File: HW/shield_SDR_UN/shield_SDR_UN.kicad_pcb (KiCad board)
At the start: 2 copper layers, 100 x 100 mm, 221 parts, among them J1 Conn_02x09_Odd_Even, J2 Conn_02x08_Odd_Even, J3 Conn_02x10_Top_Bottom, J4 USB_B_Micro, J5 USB_A, J6 Conn_02x06_Odd_Even, P1 GSG-RF-CONN, P2 GSG-RF-CONN, Q1 MOSFET_P, T1 BALUN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

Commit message: PCB route V2
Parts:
- moved R55 6.41 mm to (301.1, 78.6)
- moved C109 4.84 mm to (300.9, 77.1)
- moved C73 4.38 mm to (300.9, 99.0)
- moved C80 4.32 mm to (300.9, 97.5)
- moved C64 4.30 mm to (296.4, 106.0), turned to 0 degrees
- moved C79 4.29 mm to (300.9, 95.9)
- moved C78 2.66 mm to (302.2, 93.2)
- moved C70 2.14 mm to (277.8, 105.9)
- moved C76 2.14 mm to (285.3, 105.9)
- moved C56 2.14 mm to (282.3, 105.9)
- moved C57 2.14 mm to (283.8, 105.9)
- moved C58 2.14 mm to (280.8, 105.9)
- moved C60 2.14 mm to (279.3, 105.9)
- moved C108 1.47 mm to (302.2, 89.9)
- moved C59 1.19 mm to (276.3, 105.9)
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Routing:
- net /FPGA/FPGA_GPIO_00: track 0.00 -> 34.5 mm, vias 0 -> 2
- net /FPGA/FPGA_GPIO_01: track 0.00 -> 33.5 mm, vias 0 -> 2
- net /FPGA/FPGA_GPIO_02: track 0.00 -> 31.6 mm, vias 0 -> 2
- net I2C_SDA: track 24.0 -> 49.9 mm, vias 0 -> 3
- net 3V3 FPGA: track 0.00 -> 24.3 mm
- net I2C_SCL: track 20.6 -> 42.7 mm, vias 0 -> 3
- net /FPGA/FPGA_GPIO_03: track 13.6 -> 29.8 mm, vias 1 -> 2
- net /FPGA/FPGA_GPIO_19: track 0.00 -> 16.1 mm, vias 0 -> 2
- net /FPGA/FPGA_GPIO_18: track 0.00 -> 16.0 mm, vias 0 -> 2
- net /FPGA/FPGA_GPIO_16: track 0.00 -> 15.3 mm, vias 0 -> 2
- net /FPGA/FPGA_GPIO_20: track 0.00 -> 15.3 mm, vias 0 -> 2
- net /FPGA/FPGA_GPIO_14: track 0.00 -> 15.2 mm, vias 0 -> 2
- net /FPGA/FPGA_GPIO_21: track 0.00 -> 14.9 mm, vias 0 -> 2
- net /FPGA/FPGA_GPIO_17: track 0.00 -> 14.8 mm, vias 0 -> 2
- net /FPGA/FPGA_GPIO_15: track 0.00 -> 14.7 mm, vias 0 -> 2
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
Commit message: PCB routing
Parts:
- moved R3 0.14 mm to (237.9, 72.6), turned to 270 degrees
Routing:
- net /proc/LED2: track 0.00 -> 10.5 mm
- net /proc/LED1: track 0.00 -> 10.3 mm
- net 1V2 FPGA: track 5.49 -> 14.5 mm
- net 3V3 FPGA: track 24.3 -> 33.2 mm
- net /rf_front_end/RXBBI+: track 0.00 -> 5.61 mm
- net /rf_front_end/RXBBI-: track 0.00 -> 5.19 mm
- net /rf_front_end/RXBBQ-: track 0.00 -> 4.07 mm
- net /rf_front_end/RXBBQ+: track 0.00 -> 3.65 mm
- net /omega_2/BOOT_0: track 3.44 -> 0.04 mm
- net Net-(D6-Pad2): track 0.00 -> 2.05 mm
- net Net-(D9-Pad2): track 0.00 -> 2.05 mm
- net SPI1_MISO: track 0.00 -> 2.02 mm
- net Net-(D5-Pad2): track 0.00 -> 2.01 mm
- net Net-(D8-Pad2): track 0.00 -> 1.92 mm
- net Net-(D7-Pad2): track 0.00 -> 1.82 mm
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
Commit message: PCB route V3
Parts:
- R53: moved to B.Cu
- moved C102 155.3 mm to (115.7, 82.4)
- moved C95 155.0 mm to (116.0, 70.9)
- moved U4 155.0 mm to (131.7, 78.7)
- moved U5 155.0 mm to (131.7, 78.7)
- moved BT1 155.0 mm to (158.9, 55.0)
- moved C1 155.0 mm to (115.6, 41.9)
- moved C10 155.0 mm to (103.7, 61.9)
- moved C103 155.0 mm to (123.0, 57.9)
- moved C106 155.0 mm to (127.5, 96.3)
- moved C108 155.0 mm to (147.7, 77.9)
- moved C109 155.0 mm to (146.4, 65.2)
- moved C112 155.0 mm to (137.9, 62.8)
- moved C113 155.0 mm to (153.5, 127.0)
- moved C116 155.0 mm to (158.8, 127.0)
- moved C117 155.0 mm to (138.6, 124.0)
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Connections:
- R3 pad 2: SPI1_MOSI -> /proc/SPI1_MOSI
- U4 pad 112: /proc/FMC_NBL0 -> FMC_NBL0
- U4 pad 132: /proc/FMC_NWAIT -> FMC_NWAIT
- U4 pad 133: /proc/FMC_NWE -> FMC_NWE
- U4 pad 44: /proc/FMC_D10 -> FMC_D10
- U5 pad 1: /FPGA/FMC_A23 -> FMC_A23
- U5 pad 114: /FPGA/FMC_D2 -> FMC_D2
- U5 pad 115: /FPGA/FMC_D3 -> FMC_D3
- U5 pad 117: /FPGA/FMC_CLK -> FMC_CLK
- U5 pad 118: /FPGA/FMC_NOE -> FMC_NOE
- U5 pad 123: /FPGA/FMC_NE1 -> FMC_NE1
- U5 pad 137: /FPGA/FMC_NL -> FMC_NL
- U5 pad 142: /FPGA/FMC_NBL1 -> FMC_NBL1
- U5 pad 2: /FPGA/FMC_A19 -> FMC_A19
- U5 pad 3: /FPGA/FMC_A20 -> FMC_A20
- U5 pad 4: /FPGA/FMC_A21 -> FMC_A21
- U5 pad 43: /rf_front_end/SPI1_MOSI -> SPI1_MOSI
- U5 pad 5: /FPGA/FMC_A22 -> FMC_A22
- U5 pad 58: /FPGA/FMC_D4 -> FMC_D4
- U5 pad 59: /FPGA/FMC_D5 -> FMC_D5
- U5 pad 60: /FPGA/FMC_D6 -> FMC_D6
- U5 pad 63: /FPGA/FMC_D7 -> FMC_D7
- U5 pad 64: /FPGA/FMC_D8 -> FMC_D8
- U5 pad 65: /FPGA/FMC_D9 -> FMC_D9
- U5 pad 67: /FPGA/FMC_D11 -> FMC_D11
- U5 pad 68: /FPGA/FMC_D12 -> FMC_D12
- U5 pad 77: /FPGA/FMC_D13 -> FMC_D13
- U5 pad 78: /FPGA/FMC_D14 -> FMC_D14
- U5 pad 79: /FPGA/FMC_D15 -> FMC_D15
- U5 pad 80: /FPGA/FMC_A16 -> FMC_A16
- U5 pad 81: /FPGA/FMC_A17 -> FMC_A17
- U5 pad 82: /FPGA/FMC_A18 -> FMC_A18
- U5 pad 85: /FPGA/FMC_D0 -> FMC_D0
- U5 pad 86: /FPGA/FMC_D1 -> FMC_D1
- U5 pad 89: /FPGA/FMC_A14 -> FMC_A14
- U5 pad 90: /FPGA/FMC_A15 -> FMC_A15
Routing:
- net 3V3 FPGA: track 33.2 -> 79.8 mm
- net 3V3 MCU: track 1.64 -> 35.7 mm
- net 1V2 FPGA: track 14.5 -> 23.1 mm
- net /FPGA/DONE: track 0.00 -> 8.38 mm, vias 0 -> 1
- net FMC_A21: track 0.00 -> 8.22 mm, vias 0 -> 1
- net FMC_A17: track 0.00 -> 7.73 mm, vias 0 -> 1
- net FMC_A14: track 0.00 -> 7.49 mm, vias 0 -> 1
- net FMC_NWE: track 0.00 -> 7.31 mm, vias 0 -> 1
- net FMC_A15: track 0.00 -> 7.30 mm, vias 0 -> 1
- net FMC_A16: track 0.00 -> 7.30 mm, vias 0 -> 1
- net FMC_A19: track 0.00 -> 7.28 mm, vias 0 -> 1
- net FMC_A20: track 0.00 -> 7.21 mm, vias 0 -> 1
- net FMC_D15: track 0.00 -> 7.09 mm, vias 0 -> 1
- net FMC_D14: track 0.00 -> 7.09 mm, vias 0 -> 1
- net FMC_D13: track 0.00 -> 7.09 mm, vias 0 -> 1
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
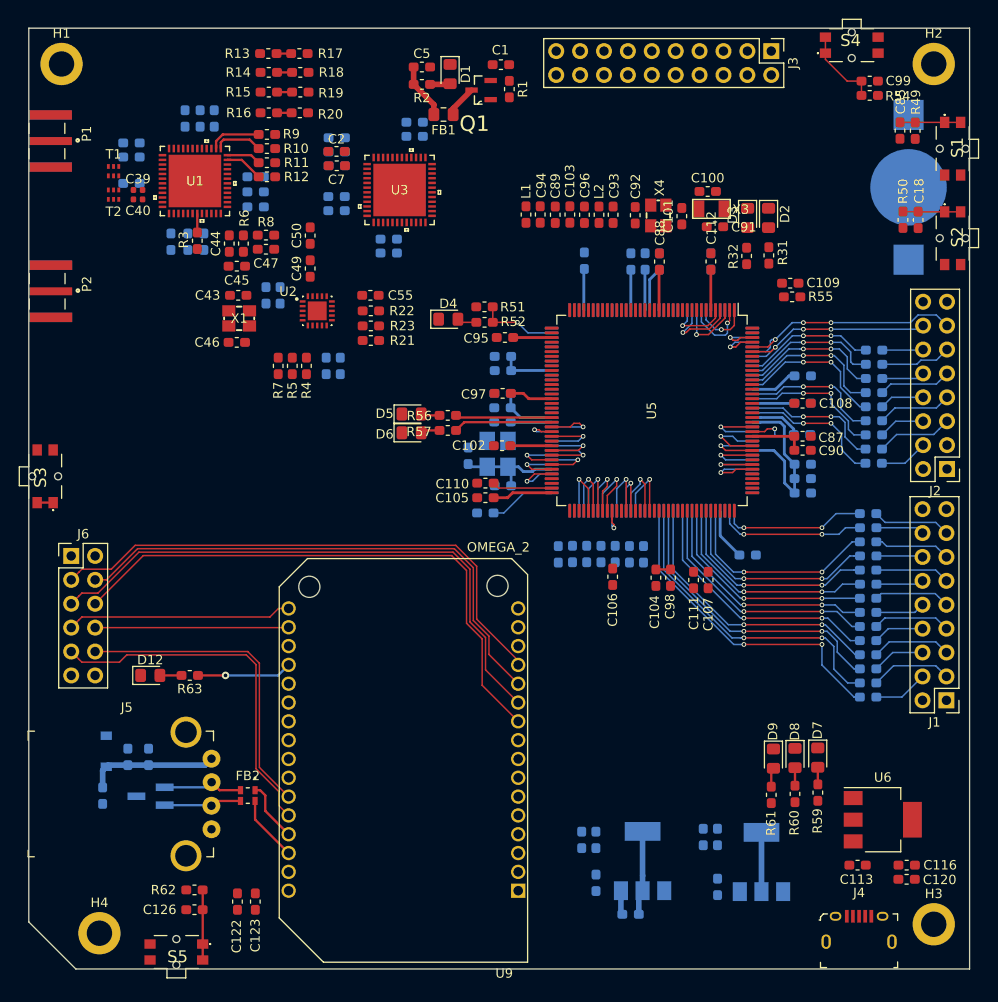
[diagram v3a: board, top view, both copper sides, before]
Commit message: PCB, Power stage routed
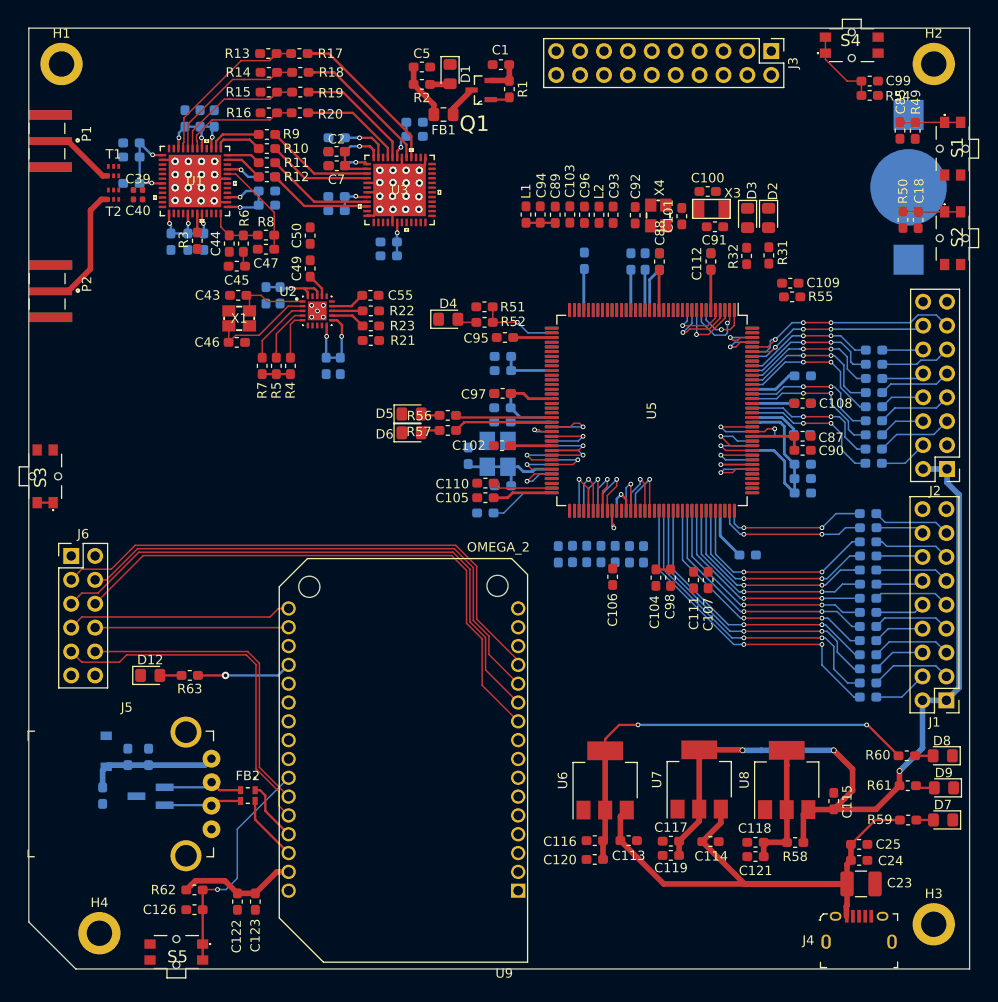
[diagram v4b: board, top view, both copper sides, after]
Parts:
- added C23: 220uF, Resistor_SMD:R_1210_3225Metric_Pad1.42x2.65mm_HandSolder, F.Cu at (153.9, 129.0)
- added C24: 100nF, Capacitor_SMD:C_0603_1608Metric_Pad1.05x0.95mm_HandSolder, F.Cu at (153.7, 126.5)
- added C25: 1nF, Capacitor_SMD:C_0603_1608Metric_Pad1.05x0.95mm_HandSolder, F.Cu at (153.7, 124.8)
- C114, C115, C117, C118, C119, C121, R58, U7, U8: moved to F.Cu
- moved C116 33.3 mm to (125.6, 124.4)
- moved C120 33.2 mm to (125.6, 126.4)
- moved U6 29.8 mm to (126.7, 118.0), turned to 90 degrees
- moved C115 26.7 mm to (151.0, 120.2)
- moved C113 24.5 mm to (129.2, 124.4)
- moved R58 19.1 mm to (146.9, 124.6), turned to 0 degrees
- moved C121 18.6 mm to (142.7, 126.1), turned to 180 degrees
- moved D9 18.4 mm to (162.7, 118.8), turned to 180 degrees
- moved U8 17.6 mm to (146.0, 118.0)
- moved C118 17.0 mm to (142.7, 124.6), turned to 180 degrees
- moved D8 15.7 mm to (162.6, 115.4), turned to 180 degrees
- moved D7 14.9 mm to (162.6, 122.2), turned to 180 degrees
- moved R61 14.5 mm to (158.9, 118.6), turned to 0 degrees
- moved R60 12.6 mm to (158.8, 115.4), turned to 0 degrees
- moved U7 11.0 mm to (136.7, 117.9)
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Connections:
- net /FPGA/FPGA_JTDO renamed /FPGA_JTDO
- net /omega_2/BOOT_0 renamed /BOOT_0
- net /omega_2/OMG_JNRST renamed /OMG_JNRST
- net /omega_2/OMG_JTCK renamed /OMG_JTCK
- net /omega_2/OMG_JTDI renamed /OMG_JTDI
- net /omega_2/OMG_JTMS renamed /OMG_JTMS
- net /omega_2/OMG_JTRST renamed /OMG_JTRST
- net /proc/STM_JTDO renamed /STM_JTDO
- R3 pad 2: /proc/SPI1_MOSI -> SPI1_MOSI
- R4 pad 2: /omega_2/I2C1_SDA -> I2C_SCL
- R5 pad 2: /omega_2/I2C1_SCL -> I2C_SDA
- U2 pad 4: /omega_2/I2C1_SCL -> I2C_SDA
- U2 pad 5: /omega_2/I2C1_SDA -> I2C_SCL
- U5 pad 40: /rf_front_end/SPI1_CS_RF -> SPI1_CS_RF
- U5 pad 41: /rf_front_end/SPI1_SCK -> SPI1_SCK
- U5 pad 42: /rf_front_end/SPI1_MISO -> SPI1_MISO
- U5 pad 44: /rf_front_end/SPI1_CS_AD -> SPI1_CS_AD
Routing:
- net 3V3 MCU: track 35.7 -> 125.5 mm, vias 0 -> 6
- net 3V3 FPGA: track 79.8 -> 160.6 mm, vias 0 -> 3
- net +5V: track 0.00 -> 65.4 mm
- net VAA: track 5.94 -> 57.3 mm, vias 0 -> 12
- net GND: track 0.00 -> 36.1 mm, vias 0 -> 37
- net /rf_front_end/QD+: track 0.00 -> 18.4 mm
- net /omega_2/RST_BTN: track 7.45 -> 24.6 mm, vias 0 -> 1
- net /rf_front_end/TXBBI+: track 1.55 -> 17.5 mm
- net /rf_front_end/QD-: track 0.00 -> 15.0 mm
- net /rf_front_end/TXBBI-: track 1.60 -> 16.1 mm
- net Net-(P2-Pad1): track 0.00 -> 13.7 mm
- net /rf_front_end/TXBBQ+: track 1.60 -> 14.5 mm
- net /rf_front_end/ID-: track 0.00 -> 12.8 mm
- net /rf_front_end/IA+: track 0.00 -> 11.5 mm
- net /rf_front_end/QA-: track 0.00 -> 11.5 mm
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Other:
- rule via_min_size: 0.4 -> 0.3

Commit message: PCB routing
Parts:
- moved D5 5.85 mm to (112.0, 79.3)
- moved D6 5.85 mm to (112.0, 81.3)
- moved R56 5.85 mm to (115.8, 79.5)
- moved R57 5.85 mm to (115.8, 81.1)
- moved C65 2.40 mm to (113.8, 79.7)
- moved C66 2.40 mm to (113.8, 81.2)
- moved X2 2.40 mm to (113.2, 84.6)
- moved C63 2.40 mm to (113.8, 88.0)
- moved C71 2.40 mm to (113.8, 78.1)
- moved C84 2.40 mm to (110.1, 84.8)
- moved C102 1.15 mm to (115.7, 83.6)
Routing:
- net adDA0: track 0.00 -> 34.2 mm, vias 0 -> 1
- net adDA1: track 0.00 -> 33.5 mm, vias 0 -> 1
- net adDA2: track 0.00 -> 32.8 mm, vias 0 -> 1
- net adDA3: track 0.00 -> 32.1 mm, vias 0 -> 1
- net adDA4: track 0.00 -> 31.1 mm, vias 0 -> 1
- net I2C_SCL: track 47.9 -> 78.5 mm, vias 3 -> 4
- net adDA5: track 0.00 -> 30.4 mm, vias 0 -> 1
- net adDA6: track 0.00 -> 29.7 mm, vias 0 -> 1
- net I2C_SDA: track 56.0 -> 84.7 mm, vias 3 -> 4
- net adDA7: track 0.00 -> 28.6 mm, vias 0 -> 1
- net adDD2: track 0.00 -> 26.8 mm, vias 0 -> 1
- net adDD0: track 0.00 -> 26.6 mm, vias 0 -> 1
- net adDD1: track 0.00 -> 25.9 mm, vias 0 -> 1
- net adDD3: track 0.00 -> 25.8 mm, vias 0 -> 1
- net adDD4: track 0.00 -> 25.2 mm, vias 0 -> 1
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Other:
- board text added: "Profe vea esta belleza, pongame 5"
- board text removed: "Camargo vea esta belleza, pongame 5"

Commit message: PCB route V4
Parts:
- C88: moved to B.Cu
- moved C112 7.19 mm to (144.9, 60.9)
- moved C74 7.18 mm to (144.9, 60.9)
- moved X2 6.75 mm to (107.8, 80.6)
- moved X3 5.76 mm to (141.9, 61.5)
- moved C92 5.56 mm to (134.9, 60.3), turned to 90 degrees
- moved C91 4.87 mm to (143.2, 58.6), turned to 90 degrees
- moved D2 4.80 mm to (148.9, 58.2)
- moved R31 4.80 mm to (148.9, 62.2)
- moved D3 4.80 mm to (146.6, 58.2)
- moved R32 4.80 mm to (146.5, 62.2)
- moved C100 4.37 mm to (140.5, 58.7), turned to 90 degrees
- moved C84 4.21 mm to (114.0, 86.4), turned to 180 degrees
- moved C89 4.16 mm to (121.9, 62.0)
- moved L1 4.16 mm to (118.8, 62.0)
- moved C94 4.16 mm to (120.3, 62.0)
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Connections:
- net /BOOT_0 renamed /omega_2/BOOT_0
- net /FPGA_JTDO renamed /FPGA/FPGA_JTDO
- net /OMG_JNRST renamed /omega_2/OMG_JNRST
- net /OMG_JTCK renamed /omega_2/OMG_JTCK
- net /OMG_JTDI renamed /omega_2/OMG_JTDI
- net /OMG_JTMS renamed /omega_2/OMG_JTMS
- net /OMG_JTRST renamed /omega_2/OMG_JTRST
- net /STM_JTDO renamed /proc/STM_JTDO
- J3 pad 10: GND -> /proc/GPIO_MCU_8
- J3 pad 11: 3V3 MCU -> /proc/GPIO_MCU_9
- J3 pad 12: /proc/GPIO_MCU_9 -> /proc/GPIO_MCU_10
- J3 pad 13: /proc/GPIO_MCU_10 -> /proc/GPIO_MCU_11
- J3 pad 14: /proc/GPIO_MCU_11 -> /proc/GPIO_MCU_12
- J3 pad 15: /proc/GPIO_MCU_12 -> /proc/GPIO_MCU_13
- J3 pad 16: /proc/GPIO_MCU_13 -> /proc/GPIO_MCU_14
- J3 pad 17: /proc/GPIO_MCU_14 -> /proc/GPIO_MCU_15
- J3 pad 18: /proc/GPIO_MCU_15 -> Net-(J3-Pad18)
- J3 pad 19: /proc/GPIO_MCU_16 -> GND
- J3 pad 2: /proc/GPIO_MCU_1 -> 3V3 MCU
- J3 pad 3: /proc/GPIO_MCU_2 -> /proc/GPIO_MCU_1
- J3 pad 4: /proc/GPIO_MCU_3 -> /proc/GPIO_MCU_2
- J3 pad 5: /proc/GPIO_MCU_4 -> /proc/GPIO_MCU_3
- J3 pad 6: /proc/GPIO_MCU_5 -> /proc/GPIO_MCU_4
- J3 pad 7: /proc/GPIO_MCU_6 -> /proc/GPIO_MCU_5
- J3 pad 8: /proc/GPIO_MCU_7 -> /proc/GPIO_MCU_6
- J3 pad 9: /proc/GPIO_MCU_8 -> /proc/GPIO_MCU_7
- R4 pad 2: I2C_SCL -> I2C_SDA
- R5 pad 2: I2C_SDA -> I2C_SCL
- U2 pad 4: I2C_SDA -> I2C_SCL
- U2 pad 5: I2C_SCL -> I2C_SDA
- U5 pad 136: /proc/GPIO_MCU_16 -> Net-(U5-Pad136)
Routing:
- net /omega_2/OMG_JNRST: track 8.67 -> 163.2 mm, vias 0 -> 5
- net /omega_2/OMG_JTMS: track 0.00 -> 140.5 mm, vias 0 -> 3
- net /FPGA/FPGA_JTDO: track 0.00 -> 115.1 mm, vias 0 -> 6
- net /omega_2/OMG_JTCK: track 0.00 -> 103.2 mm, vias 0 -> 6
- net /omega_2/OMG_JTRST: track 0.00 -> 79.6 mm, vias 0 -> 5
- net GCK0: track 0.00 -> 65.1 mm, vias 0 -> 5
- net /omega_2/OMG_JTDI: track 0.00 -> 59.8 mm, vias 0 -> 3
- net GCK1: track 0.00 -> 43.4 mm, vias 0 -> 3
- net UART1_RX: track 0.00 -> 42.7 mm, vias 0 -> 3
- net 3V3 MCU: track 126.1 -> 167.2 mm, vias 6 -> 7
- net UART1_TX: track 0.00 -> 40.7 mm, vias 0 -> 3
- net 3V3 FPGA: track 169.0 -> 208.4 mm
- net /proc/GPIO_MCU_11: track 0.00 -> 35.0 mm, vias 0 -> 1
- net /proc/GPIO_MCU_9: track 0.00 -> 34.3 mm, vias 0 -> 1
- net /proc/GPIO_MCU_7: track 0.00 -> 33.8 mm, vias 0 -> 1
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
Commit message: PCB routing
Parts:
- added R64: 1.5k, Resistor_SMD:R_0603_1608Metric_Pad1.05x0.95mm_HandSolder, B.Cu at (118.6, 66.9)
- added R65: 1.5k, Resistor_SMD:R_0603_1608Metric_Pad1.05x0.95mm_HandSolder, B.Cu at (117.0, 66.9)
- moved R3 3.37 mm to (83.4, 64.0)
- moved C75 0.33 mm to (115.8, 72.6)
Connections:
- J3 pad 18: Net-(J3-Pad18) -> GND
- U4 pad 60: adDA4 -> 3V3 FPGA
- U4 pad 61: adDA5 -> adDA4
- U4 pad 62: adDA6 -> adDA5
- U4 pad 64: adDA7 -> adDA6
- U4 pad 65: adDD0 -> adDA7
- U4 pad 66: adDD1 -> adDD0
- U4 pad 67: adDD2 -> adDD1
- U4 pad 69: adDD3 -> 3V3 FPGA
- U4 pad 70: adDD4 -> adDD2
- U4 pad 74: adDD5 -> adDD3
- U4 pad 75: adDD6 -> adDD4
- U4 pad 78: adDD7 -> adDD5
- U4 pad 79: adDD8 -> adDD6
- U4 pad 80: adDD9 -> adDD7
- U4 pad 81: Net-(U4-Pad81) -> adDD8
- U4 pad 82: Net-(U4-Pad82) -> adDD9
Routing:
- net adDA7: track 28.6 -> 7.85 mm
- net 3V3 FPGA: track 208.4 -> 219.8 mm, vias 5 -> 4
- net adDD2: track 26.8 -> 15.9 mm
- net adDD3: track 25.8 -> 15.2 mm
- net adDD0: track 26.6 -> 16.7 mm
- net adDD1: track 25.9 -> 16.2 mm
- net adDD4: track 25.2 -> 15.6 mm
- net SPI1_MISO: track 2.02 -> 5.40 mm
- net adDA6: track 29.7 -> 28.8 mm
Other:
- net class Default: trace_width 0.25 -> 0.16; via_dia 0.8 -> 0.5; via_drill 0.4 -> 0.3

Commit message: PCB_VERSION2
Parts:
- added J7: Conn_01x03_Male, Connector_PinHeader_2.54mm:PinHeader_1x03_P2.54mm_Vertical, F.Cu at (145.4, 50.6)
- moved C75 1.65 mm to (115.8, 70.9)
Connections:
- BT1 pad 1: 3V3 MCU -> Net-(BT1-Pad1)
- C112 pad 1: 3V3 MCU -> Net-(C112-Pad1)
- U5 pad 35: rf_RSSI -> rf_ANTSEL
- U5 pad 40: SPI1_CS_RF -> SPI1_CS_AD
- U5 pad 44: SPI1_CS_AD -> SPI1_CS_RF
- U5 pad 46: rf_ANTSEL -> rf_LD
- U5 pad 47: rf_!SHDN -> rf_RSSI
- U5 pad 48: rf_LD -> GPIO_CLK
- U5 pad 49: GPIO_INTR -> MCU_CLK
- U5 pad 50: MCU_CLK -> GPIO_INTR
- U5 pad 53: GPIO_CLK -> rf_!SHDN
- U5 pad 6: 3V3 MCU -> Net-(C112-Pad1)
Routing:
- net SPI1_SCK: track 0.00 -> 89.8 mm, vias 0 -> 6
- net SPI1_MISO: track 5.40 -> 90.0 mm, vias 0 -> 6
- net rf_RSSI: track 0.00 -> 62.2 mm, vias 0 -> 6
- net SPI1_CS_RF: track 0.00 -> 58.8 mm, vias 0 -> 4
- net rf_!SHDN: track 14.3 -> 63.8 mm, vias 0 -> 2
- net SPI1_MOSI: track 0.00 -> 49.4 mm, vias 0 -> 4
- net rf_LD: track 14.6 -> 61.0 mm, vias 0 -> 4
- net SPI1_CS_AD: track 0.00 -> 32.7 mm, vias 0 -> 2
- net Net-(BT1-Pad1): track 0.00 -> 26.5 mm
- net Net-(C112-Pad1): track 0.00 -> 25.8 mm, vias 0 -> 2
- net GPIO_INTR: track 22.3 -> 46.7 mm, vias 0 -> 2
- net adDA7: track 7.85 -> 27.5 mm
- net rf_ANTSEL: track 13.9 -> 0.00 mm
- net adDD0: track 16.7 -> 26.4 mm
- net adDD4: track 15.6 -> 24.7 mm
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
